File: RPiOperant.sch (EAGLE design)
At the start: 59 parts, among them IC1 74LS14N, IC2 74LS14N, IC3 MCP3008, J1 USB_B_PTH, J2 POWER_JACK, J3 POWER_JACK, J4 USB_B_PTH, J5 1X2-3.5MM, J6 1X2-3.5MM, J7 1X2-3.5MM, J8 1X2-3.5MM, J9 1X2-3.5MM

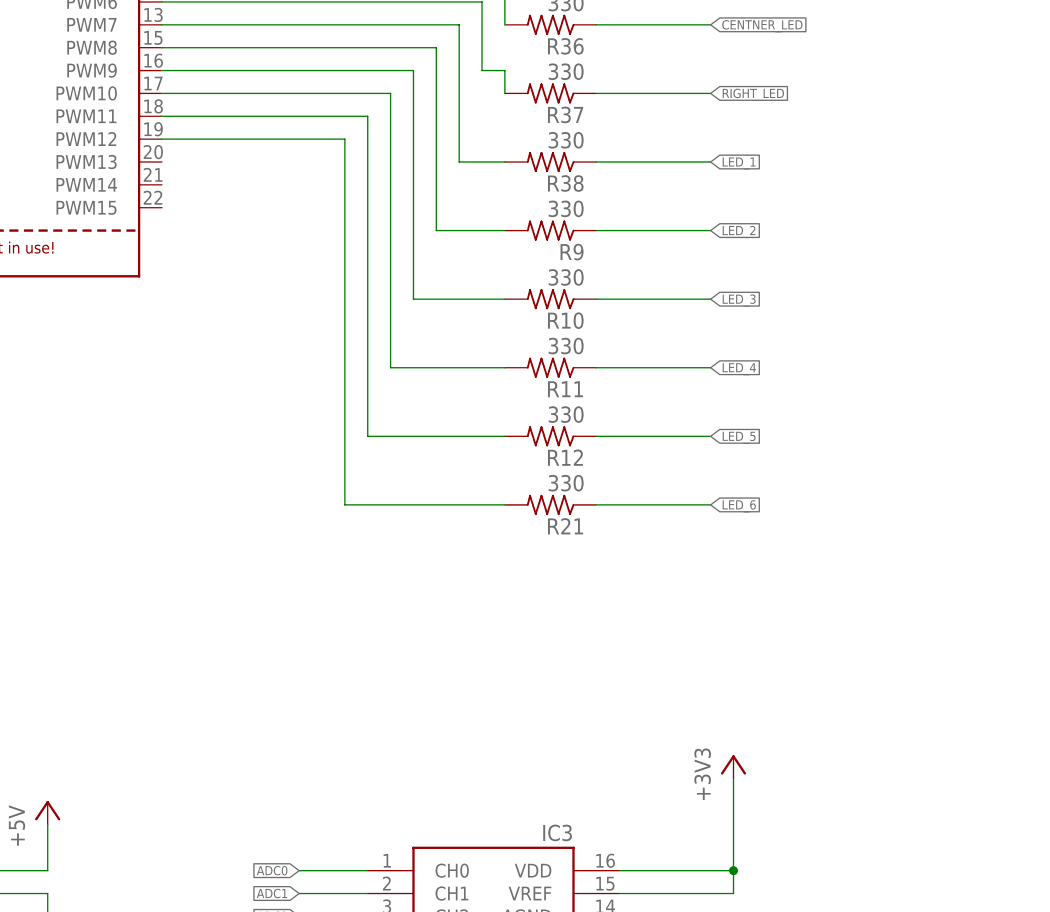
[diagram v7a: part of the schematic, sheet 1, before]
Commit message: board labesl
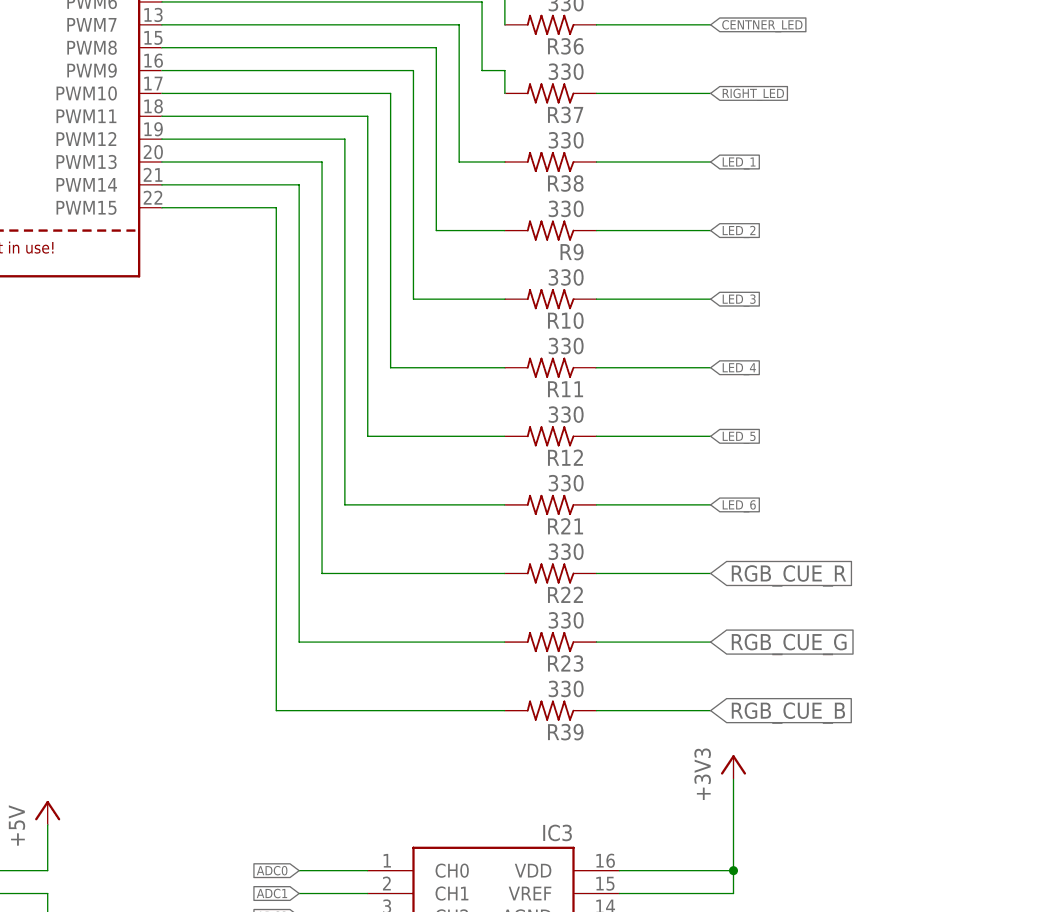
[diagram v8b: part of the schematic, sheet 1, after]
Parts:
- added R22, R23, R39: 330, resistor:R-US_0207/7
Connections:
- new net N$19: R22.2, U1.PWM13
- new net N$20: R23.2, U1.PWM14
- new net N$21: R39.2, U1.PWM15
- net RGB_CUE_B: now also R39.1
- net RGB_CUE_G: now also R23.1
- net RGB_CUE_R: now also R22.1
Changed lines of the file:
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@@
 <part name="R21" library="resistor" library_urn="urn:adsk.eagle:library:348" deviceset="R-US_" device="0207/7" package3d_urn="urn:adsk.eagle:package:25942/1" value="330"/>
 <part name="GND15" library="SparkFun-PowerSymbols" deviceset="GND" device=""/>
+<part name="R22" library="resistor" library_urn="urn:adsk.eagle:library:348" deviceset="R-US_" device="0207/7" package3d_urn="urn:adsk.eagle:package:25942/1" value="330"/>
+<part name="R23" library="resistor" library_urn="urn:adsk.eagle:library:348" deviceset="R-US_" device="0207/7" package3d_urn="urn:adsk.eagle:package:25942/1" value="330"/>
+<part name="R39" library="resistor" library_urn="urn:adsk.eagle:library:348" deviceset="R-US_" device="0207/7" package3d_urn="urn:adsk.eagle:package:25942/1" value="330"/>
 </parts>
 <sheets>
@@
 <instance part="R21" gate="G$1" x="53.34" y="180.34" rot="R180"/>
 <instance part="GND15" gate="1" x="-218.44" y="193.04"/>
+<instance part="R22" gate="G$1" x="53.34" y="172.72" rot="R180"/>
+<instance part="R23" gate="G$1" x="53.34" y="165.1" rot="R180"/>
+<instance part="R39" gate="G$1" x="53.34" y="157.48" rot="R180"/>
 </instances>
 <busses>
@@
 <label x="-101.6" y="152.4" size="1.016" layer="91" rot="R90" xref="yes"/>
 </segment>
+<segment>
+<pinref part="R22" gate="G$1" pin="1"/>
+<wire x1="58.42" y1="172.72" x2="71.12" y2="172.72" width="0.1524" layer="91"/>
+<label x="71.12" y="172.72" size="1.778" layer="91" xref="yes"/>
+</segment>
 </net>
 <net name="RGB_CUE_B" class="0">
@@
 <label x="-99.06" y="152.4" size="1.016" layer="91" rot="R90" xref="yes"/>
 </segment>
+<segment>
+<pinref part="R39" gate="G$1" pin="1"/>
+<wire x1="58.42" y1="157.48" x2="71.12" y2="157.48" width="0.1524" layer="91"/>
+<label x="71.12" y="157.48" size="1.778" layer="91" xref="yes"/>
+</segment>
 </net>
 <net name="RGB_CUE_G" class="0">
@@
 <wire x1="-96.52" y1="144.78" x2="-96.52" y2="152.4" width="0.1524" layer="91"/>
 <label x="-96.52" y="152.4" size="1.016" layer="91" rot="R90" xref="yes"/>
+</segment>
+<segment>
+<pinref part="R23" gate="G$1" pin="1"/>
+<wire x1="58.42" y1="165.1" x2="71.12" y2="165.1" width="0.1524" layer="91"/>
+<label x="71.12" y="165.1" size="1.778" layer="91" xref="yes"/>
 </segment>
 </net>
@@
 </segment>
 </net>
+<net name="N$19" class="0">
+<segment>
+<pinref part="U1" gate="G$1" pin="PWM13"/>
+<wire x1="10.16" y1="218.44" x2="27.94" y2="218.44" width="0.1524" layer="91"/>
+<wire x1="27.94" y1="218.44" x2="27.94" y2="172.72" width="0.1524" layer="91"/>
+<pinref part="R22" gate="G$1" pin="2"/>
+<wire x1="27.94" y1="172.72" x2="48.26" y2="172.72" width="0.1524" layer="91"/>
+</segment>
+</net>
+<net name="N$20" class="0">
+<segment>
+<pinref part="U1" gate="G$1" pin="PWM14"/>
+<wire x1="10.16" y1="215.9" x2="25.4" y2="215.9" width="0.1524" layer="91"/>
+<wire x1="25.4" y1="215.9" x2="25.4" y2="165.1" width="0.1524" layer="91"/>
+<pinref part="R23" gate="G$1" pin="2"/>
+<wire x1="25.4" y1="165.1" x2="48.26" y2="165.1" width="0.1524" layer="91"/>
+</segment>
+</net>
+<net name="N$21" class="0">
+<segment>
+<pinref part="U1" gate="G$1" pin="PWM15"/>
+<wire x1="10.16" y1="213.36" x2="22.86" y2="213.36" width="0.1524" layer="91"/>
+<wire x1="22.86" y1="213.36" x2="22.86" y2="157.48" width="0.1524" layer="91"/>
+<pinref part="R39" gate="G$1" pin="2"/>
+<wire x1="22.86" y1="157.48" x2="48.26" y2="157.48" width="0.1524" layer="91"/>
+</segment>
+</net>
